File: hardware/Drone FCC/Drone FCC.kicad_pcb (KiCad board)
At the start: 2 copper layers, 99.1 x 44.4 mm, 23 parts, among them J1 Conector GPS Auxiliar, J10 Conn_01x03, J11 Conn_01x03, J12 Conn_01x03, J13 Conn_01x03, J14 Conn_01x03, J15 Conn_01x03, J16 Conn_01x03, J17 Conn_01x04, J18 Conn_01x04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

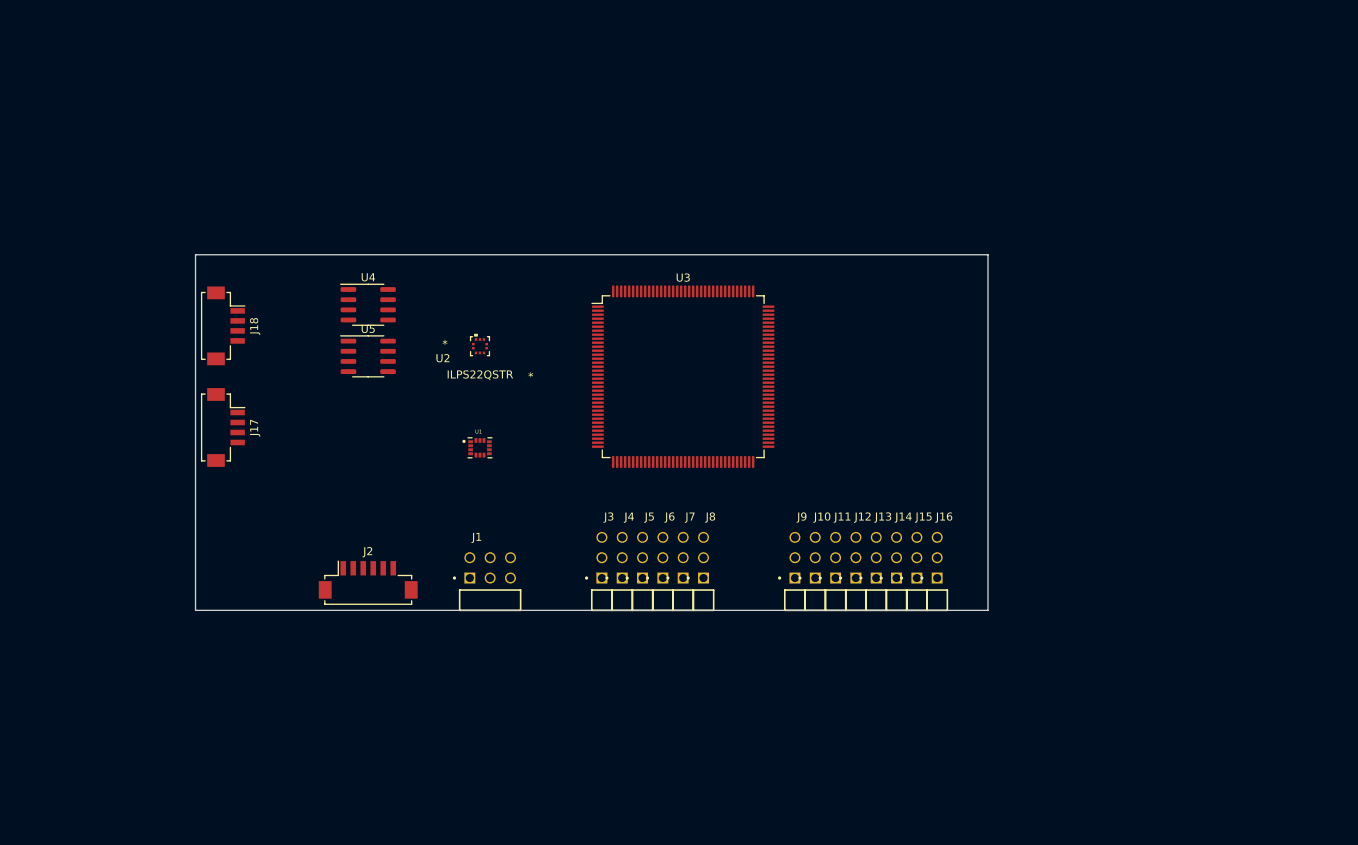
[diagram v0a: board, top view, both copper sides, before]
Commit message: add USB connector
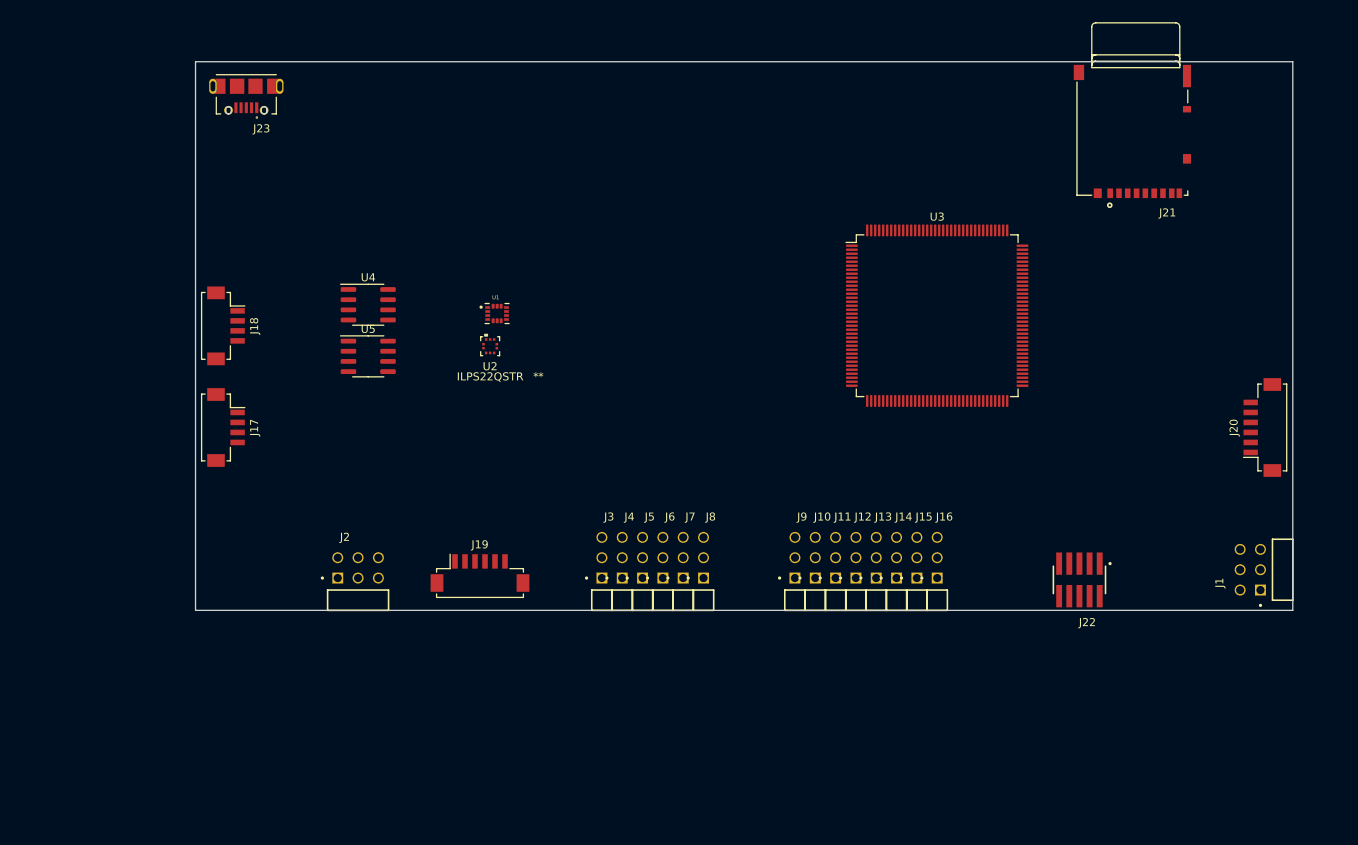
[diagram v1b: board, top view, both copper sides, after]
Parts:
- added J19: GPS M8N, Connector_Hirose:Hirose_DF13C_CL535-0406-3-51_1x06-1MP_P1.25mm_Vertical, F.Cu at (118.1, 95.7)
- added J20: Conector Magnetómetro I2C DF13, Connector_Hirose:Hirose_DF13C_CL535-0406-3-51_1x06-1MP_P1.25mm_Vertical, F.Cu at (215.9, 77.5)
- added J21: Micro_SD_Card_Det_Hirose_DM3AT, DM3AT-SF-PEJM5:HRS_DM3AT-SF-PEJM5, F.Cu at (200.1, 48.2)
- added J22: Conn_02x05_Odd_Even, FTSH-105-01-F-DV-K-TR:SAMTEC_FTSH-105-01-F-DV-P-TR, F.Cu at (193.0, 96.5)
- added J23: 47589-0001, 47589-0001:MOLEX_47589-0001, F.Cu at (88.9, 35.6)
- J1: value Conector GPS Auxiliar -> Conn_02x03_Counter_Clockwise
- J2: value GPS M8N -> Conector GPS Auxiliar; footprint Connector_Hirose:Hirose_DF13C_CL535-0406-3-51_1x06-1MP_P1.25mm_Vertical -> TSW-103-08-G-D-RA:SAMTEC_TSW-103-08-G-D-RA
- moved J1 99.1 mm to (218.4, 95.2), turned to 90 degrees
- moved U3 32.7 mm to (175.3, 63.5)
- moved U1 16.9 mm to (120.2, 63.2)
- moved J2 2.84 mm to (102.9, 99.1)
- moved U2 1.27 mm to (119.4, 67.3)
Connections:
- net /IMU/IMU_CS renamed /Sensores/IMU_CS
- J2 pad 1: GND -> /USART1_TX
- J2 pad 2: /Modulo_GNSS/GNSS_SDA -> /USART1_RX
- J2 pad 3: /Modulo_GNSS/GNSS_SCL -> GND
- J2 pad 4: /Modulo_GNSS/GNSS_Rx -> 3V3
- J2 pad 5: /Modulo_GNSS/GNSS_Tx -> 5V
- J2 pad 6: 5V -> /USART1_CK
- U1 pad 13: /IMU/IMU_CLK -> /SPI1_SCK
- U1 pad 14: /IMU/IMU_MOSI -> /SPI1_MOSI
- U3 pad 100: unconnected-(U3-Pad100) -> /USART1_CK
- U3 pad 101: unconnected-(U3-Pad101) -> /USART1_TX
- U3 pad 102: unconnected-(U3-Pad102) -> /USART1_RX
- U3 pad 114: unconnected-(U3-Pad114) -> /CAN1_RX
- U3 pad 115: unconnected-(U3-Pad115) -> /CAN1_TX
- U3 pad 135: unconnected-(U3-Pad135) -> /CAN2_RX
- U3 pad 136: unconnected-(U3-Pad136) -> /CAN2_TX
- U3 pad 41: unconnected-(U3-Pad41) -> /SPI1_SCK
- U3 pad 42: unconnected-(U3-Pad42) -> /SPI1_MISO
- U3 pad 43: unconnected-(U3-Pad43) -> /SPI1_MOSI
- U3 pad 53: unconnected-(U3-Pad53) -> /I2C4_SMBA
- U3 pad 54: unconnected-(U3-Pad54) -> /I2C4_SCL
- U3 pad 55: unconnected-(U3-Pad55) -> /I2C4_SDA
- U3 pad 60: unconnected-(U3-Pad60) -> /PWM5
- U3 pad 64: unconnected-(U3-Pad64) -> /PWM6
- U3 pad 66: unconnected-(U3-Pad66) -> /PWM7
- U3 pad 67: unconnected-(U3-Pad67) -> /PWM8
- U3 pad 69: unconnected-(U3-Pad69) -> /I2C2_SCL
- U3 pad 70: unconnected-(U3-Pad70) -> /I2C2_SDA
- U3 pad 81: unconnected-(U3-Pad81) -> /PWM1
- U3 pad 82: unconnected-(U3-Pad82) -> /PWM2
- U3 pad 85: unconnected-(U3-Pad85) -> /PWM3
- U3 pad 86: unconnected-(U3-Pad86) -> /PWM4
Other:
- board size 99.1 x 44.4 mm -> 137.2 x 68.6 mm

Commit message: DSM: deleted dupont conn, PPM: deleted DF-13 conn
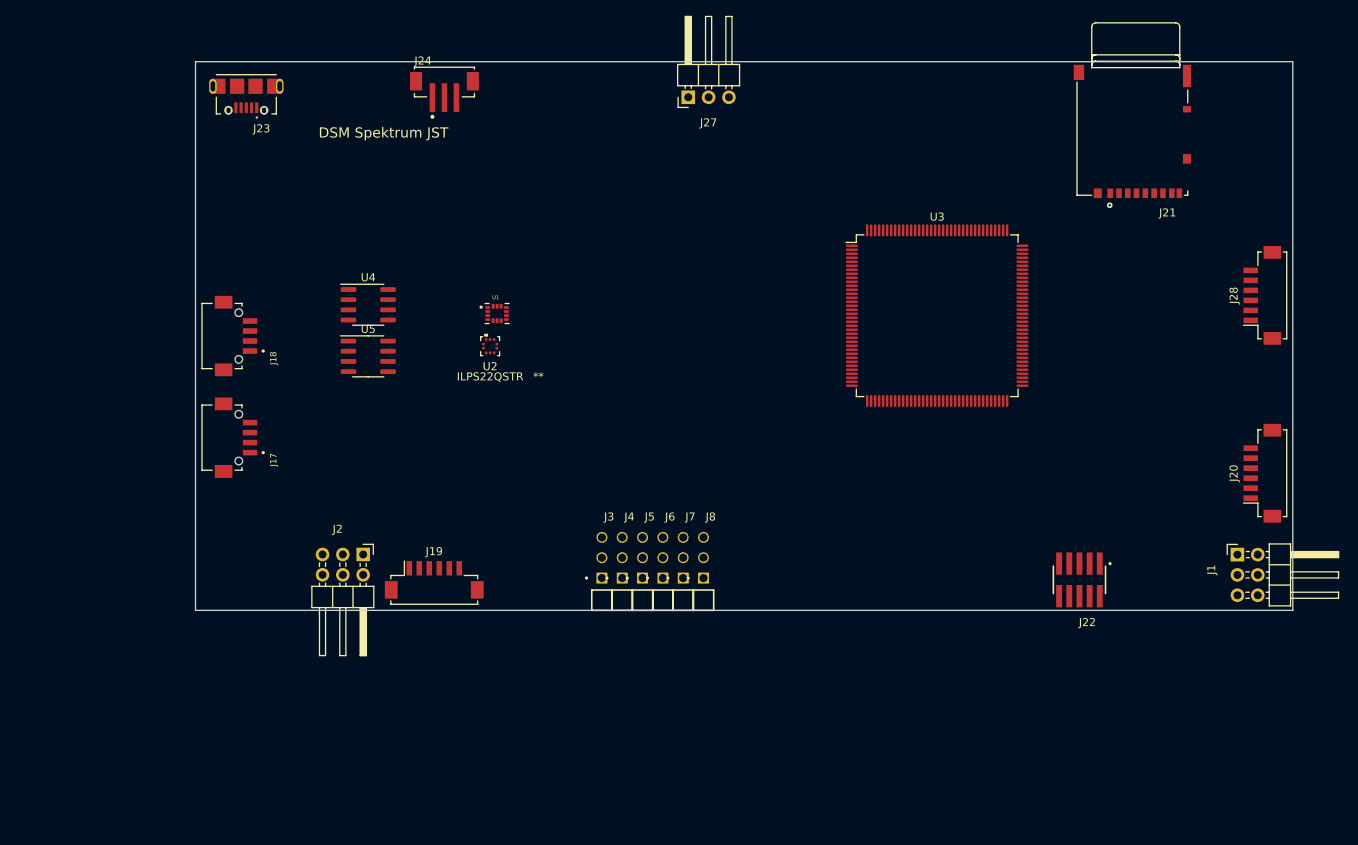
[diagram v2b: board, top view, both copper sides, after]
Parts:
- removed J10, J11, J12, J13, J14, J15, J16, J9: Conn_01x03, TSW-101-08-G-T-RA:SAMTEC_TSW-101-08-G-T-RA
- added J24: DSM Spektrum JST, B3B-ZR-SM4-TF(LF)(SN):JST-B3B-ZR-SM4-TFLFSN-0-0-MFG, F.Cu at (113.7, 34.3)
- added J27: PPM Dupont, Connector_PinHeader_2.54mm:PinHeader_1x03_P2.54mm_Horizontal, F.Cu at (144.1, 36.2)
- added J28: Conn_01x06, Connector_Hirose:Hirose_DF13C_CL535-0406-3-51_1x06-1MP_P1.25mm_Vertical, F.Cu at (215.9, 61.0)
- J1, J2: footprint TSW-103-08-G-D-RA:SAMTEC_TSW-103-08-G-D-RA -> Connector_PinHeader_2.54mm:PinHeader_2x03_P2.54mm_Horizontal
- J17, J18: footprint Connector_Hirose:Hirose_DF13C_CL535-0404-8-51_1x04-1MP_P1.25mm_Vertical -> DF13-4P-1.25H:HRS_DF13-4P-1.25H(75)
- moved J1 5.96 mm to (212.8, 93.4), turned to 0 degrees
- moved J19 5.78 mm to (112.4, 96.5)
- moved J2 5.75 mm to (103.5, 93.3), turned to -90 degrees
- moved J20 5.72 mm to (215.9, 83.2)
- moved J18 2.04 mm to (88.0, 66.0), turned to 90 degrees
- moved J17 2.04 mm to (88.0, 78.7), turned to 90 degrees

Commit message: changed mag connector for GPS module DF-13
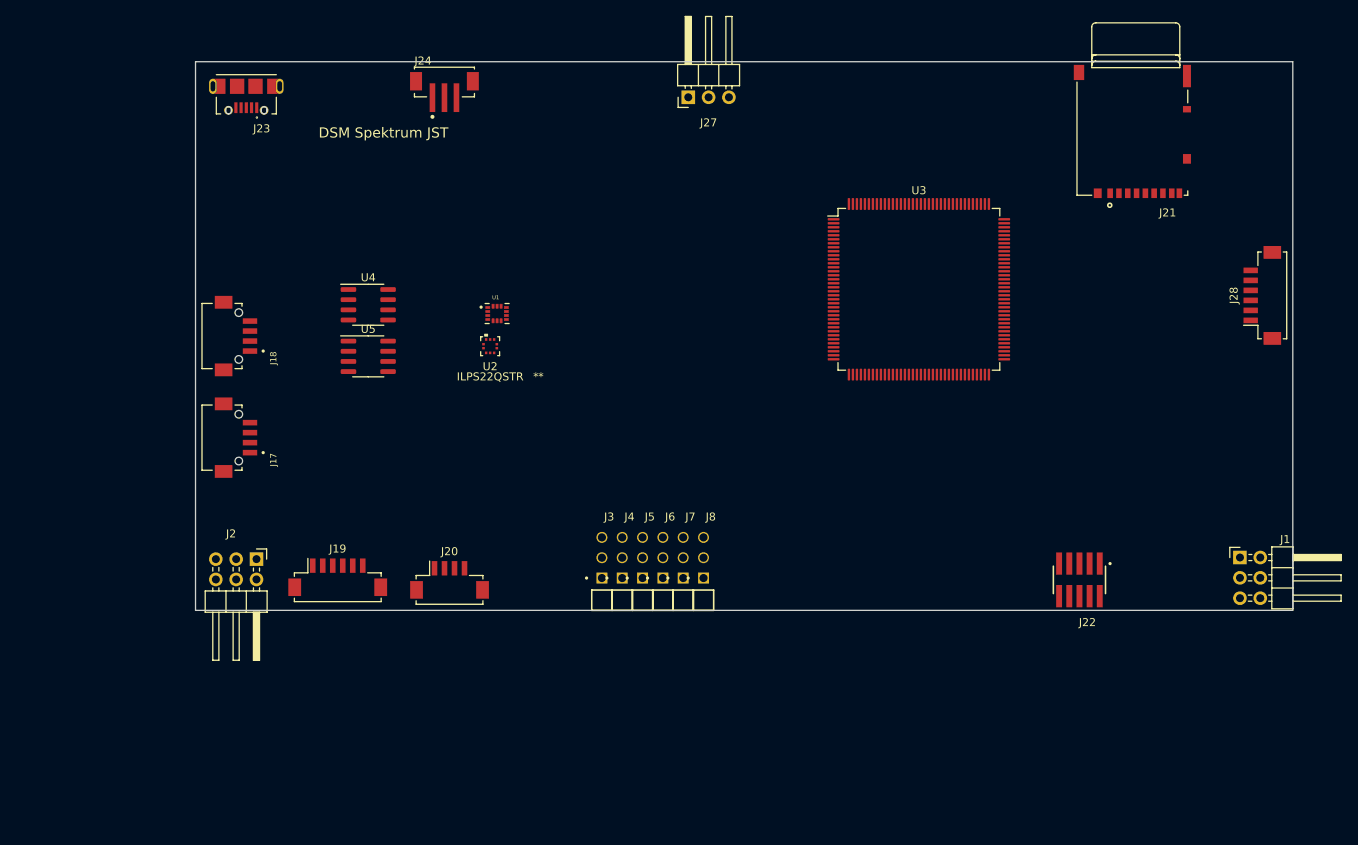
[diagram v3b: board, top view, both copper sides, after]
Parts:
- J1: value Conn_02x03_Counter_Clockwise -> Mag Dupont
- J19: value GPS M8N -> GPS M8N - DF13
- J2: value Conector GPS Auxiliar -> GPS Dupont
- J20: value Conector Magnetómetro I2C DF13 -> Mag DF13; footprint Connector_Hirose:Hirose_DF13C_CL535-0406-3-51_1x06-1MP_P1.25mm_Vertical -> Connector_Hirose:Hirose_DF13C_CL535-0404-8-51_1x04-1MP_P1.25mm_Vertical
- moved J20 102.5 mm to (114.3, 96.5), turned to 0 degrees
- moved J2 13.3 mm to (90.2, 93.9)
- moved J19 12.1 mm to (100.3, 96.2)
- moved U3 4.02 mm to (173.0, 60.2)
- moved J1 0.48 mm to (213.1, 93.7)
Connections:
- net /CAN1_RX renamed /MCU/CAN1_RX
- net /CAN1_TX renamed /MCU/CAN1_TX
- net /CAN2_RX renamed /MCU/CAN2_RX
- net /CAN2_TX renamed /MCU/CAN2_TX
- net /I2C4_SMBA renamed /MCU/I2C4_SMBA
- net /PWM7 renamed /MCU/PWM9
- net /PWM8 renamed /MCU/PWM8
- net Net-(R6-Pad1) renamed /Sensores/IMU_INT_DATA_RDY
- J1 pad 2: 5V -> GND
- J1 pad 3: /I2C4_SCL -> unconnected-(J1-Pad3)
- J1 pad 4: /I2C4_SDA -> 3V3
- J1 pad 5: 3V3 -> /I2C4_SCL
- J1 pad 6: GND -> /I2C4_SDA
- J2 pad 6: /USART1_CK -> /Sensores/GNSS_PPS
- J20 pad 1: /Sensores/MAG_INT_DATA_RDY -> 3V3
- J20 pad 2: 5V -> /I2C4_SCL
- J20 pad 3: /I2C4_SCL -> /I2C4_SDA
- J20 pad 4: /I2C4_SDA -> GND
- U1 pad 1: Net-(R1-Pad2) -> /SPI1_MISO
- U2 pad 2: Net-(R3-Pad2) -> /I2C2_SCL
- U2 pad 4: Net-(R2-Pad1) -> /I2C2_SDA
- U3 pad 100: /USART1_CK -> unconnected-(U3-Pad100)
- U3 pad 54: /I2C4_SCL -> /I2C4_SDA
- U3 pad 55: /I2C4_SDA -> /I2C4_SCL
- U3 pad 60: /PWM5 -> /MCU/PWM11
- U3 pad 64: /PWM6 -> /MCU/PWM10
- U3 pad 69: /I2C2_SCL -> /I2C2_SDA
- U3 pad 70: /I2C2_SDA -> /I2C2_SCL
- U3 pad 81: /PWM1 -> /MCU/PWM1
- U3 pad 82: /PWM2 -> /MCU/PWM2
- U3 pad 85: /PWM3 -> /MCU/PWM3
- U3 pad 86: /PWM4 -> /MCU/PWM4

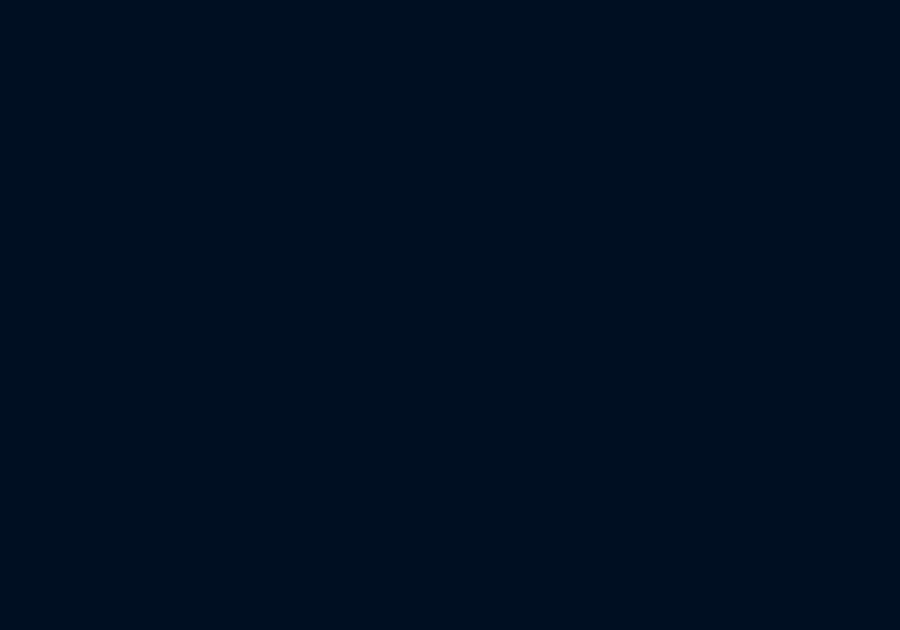
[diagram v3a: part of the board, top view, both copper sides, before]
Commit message: add LDO 3V3 to schematic
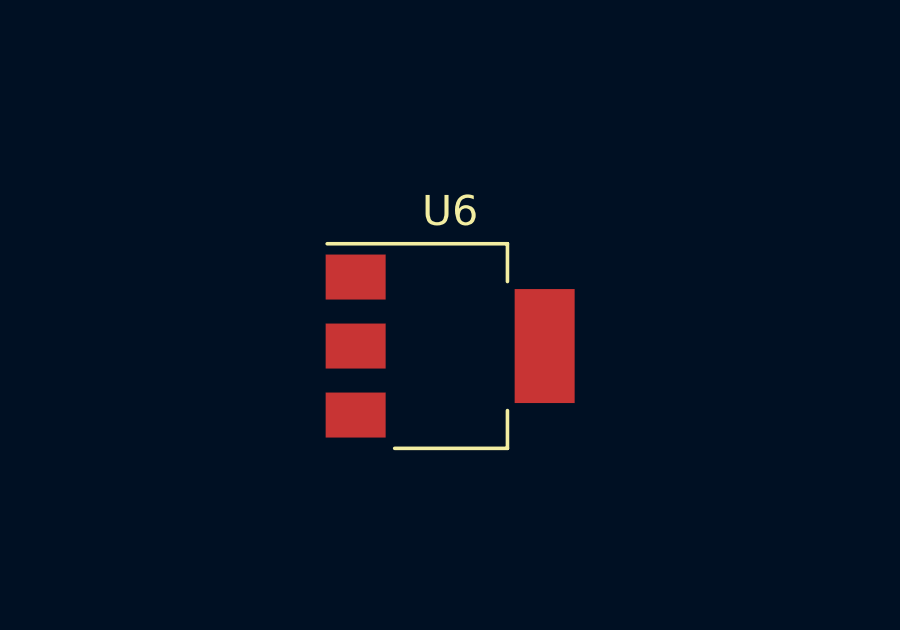
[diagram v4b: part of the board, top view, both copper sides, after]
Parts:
- added U6: ZLDO1117QG33TA, Package_TO_SOT_SMD:SOT-223-3_TabPin2, F.Cu at (172.7, 83.8)
- J28: value Conn_01x06 -> PM02 PixHawk
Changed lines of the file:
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@@
   (net 197 "/MCU/CAN2_RX")
   (net 198 "/MCU/CAN2_TX")
+  (net 199 "unconnected-(U6-Pad1)")
+  (net 200 "unconnected-(U6-Pad2)")
+  (net 201 "unconnected-(U6-Pad3)")
   (footprint "B3B-ZR-SM4-TF(LF)(SN):JST-B3B-ZR-SM4-TFLFSN-0-0-MFG" (layer "F.Cu")
     (at 113.665 34.29)
@@
     )
   )
+  (footprint "Package_TO_SOT_SMD:SOT-223-3_TabPin2" (layer "F.Cu")
+    (at 172.72 83.82)
+    (descr "module CMS SOT223 4 pins")
+    (tags "CMS SOT")
+    (property "Sheetfile" "alimentacion.kicad_sch")
+    (property "Sheetname" "Alimentación")
+    (attr smd)
+    (fp_text reference "U6" (at 0 -4.5) (layer "F.SilkS")
+      (effects (font (size 1 1) (thickness 0.15)))
+    )
+    (fp_text value "ZLDO1117QG33TA" (at 0 4.5) (layer "F.Fab")
+      (effects (font (size 1 1) (thickness 0.15)))
+    )
+    (fp_text user "${REFERENCE}" (at 0 0 90) (layer "F.Fab")
+      (effects (font (size 0.8 0.8) (thickness 0.12)))
+    )
+    (fp_line (start 1.91 -3.41) (end 1.91 -2.15) (layer "F.SilkS") (width 0.12))
+    (fp_line (start 1.91 3.41) (end 1.91 2.15) (layer "F.SilkS") (width 0.12))
+    (fp_line (start -4.1 -3.41) (end 1.91 -3.41) (layer "F.SilkS") (width 0.12))
+    (fp_line (start -1.85 3.41) (end 1.91 3.41) (layer "F.SilkS") (width 0.12))
+    (fp_line (start -4.4 3.6) (end 4.4 3.6) (layer "F.CrtYd") (width 0.05))
+    (fp_line (start 4.4 3.6) (end 4.4 -3.6) (layer "F.CrtYd") (width 0.05))
+    (fp_line (start -4.4 -3.6) (end -4.4 3.6) (layer "F.CrtYd") (width 0.05))
+    (fp_line (start 4.4 -3.6) (end -4.4 -3.6) (layer "F.CrtYd") (width 0.05))
+    (fp_line (start -1.85 -2.35) (end -1.85 3.35) (layer "F.Fab") (width 0.1))
+    (fp_line (start -0.85 -3.35) (end 1.85 -3.35) (layer "F.Fab") (width 0.1))
+    (fp_line (start -1.85 3.35) (end 1.85 3.35) (layer "F.Fab") (width 0.1))
+    (fp_line (start 1.85 -3.35) (end 1.85 3.35) (layer "F.Fab") (width 0.1))
+    (fp_line (start -1.85 -2.35) (end -0.85 -3.35) (layer "F.Fab") (width 0.1))
+    (pad "1" smd rect (at -3.15 -2.3) (size 2 1.5) (layers "F.Cu" "F.Paste" "F.Mask")
+      (net 199 "unconnected-(U6-Pad1)") (pinfunction "GND") (pintype "power_in"))
+    (pad "2" smd rect (at -3.15 0) (size 2 1.5) (layers "F.Cu" "F.Paste" "F.Mask")
+      (net 200 "unconnected-(U6-Pad2)") (pinfunction "VO") (pintype "power_out"))
+    (pad "2" smd rect (at 3.15 0) (size 2 3.8) (layers "F.Cu" "F.Paste" "F.Mask")
+      (net 200 "unconnected-(U6-Pad2)") (pinfunction "VO") (pintype "power_out"))
+    (pad "3" smd rect (at -3.15 2.3) (size 2 1.5) (layers "F.Cu" "F.Paste" "F.Mask")
+      (net 201 "unconnected-(U6-Pad3)") (pinfunction "VI") (pintype "power_in"))
+    (model "${KICAD6_3DMODEL_DIR}/Package_TO_SOT_SMD.3dshapes/SOT-223.wrl"
+      (offset (xyz 0 0 0))
+      (scale (xyz 1 1 1))
+      (rotate (xyz 0 0 0))
+    )
+  )
   (footprint "TSW-101-08-G-T-RA:SAMTEC_TSW-101-08-G-T-RA" (layer "F.Cu")
     (at 143.51 99.06)
@@
       (effects (font (size 1 1) (thickness 0.15)))
     )
-    (fp_text value "Conn_01x06" (at 0 4.15 90) (layer "F.Fab")
+    (fp_text value "PM02 PixHawk" (at 0 4.15 90) (layer "F.Fab")
       (effects (font (size 1 1) (thickness 0.15)))
     )
